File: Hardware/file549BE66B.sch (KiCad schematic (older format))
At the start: 26 parts, among them P21 CONN_01X01, P22 CONN_01X03, P23 CONN_01X01, P24 CONN_01X01, P28 CONN_01X05, U6 CONN_15, U7 LCD-jhd12864e-xl

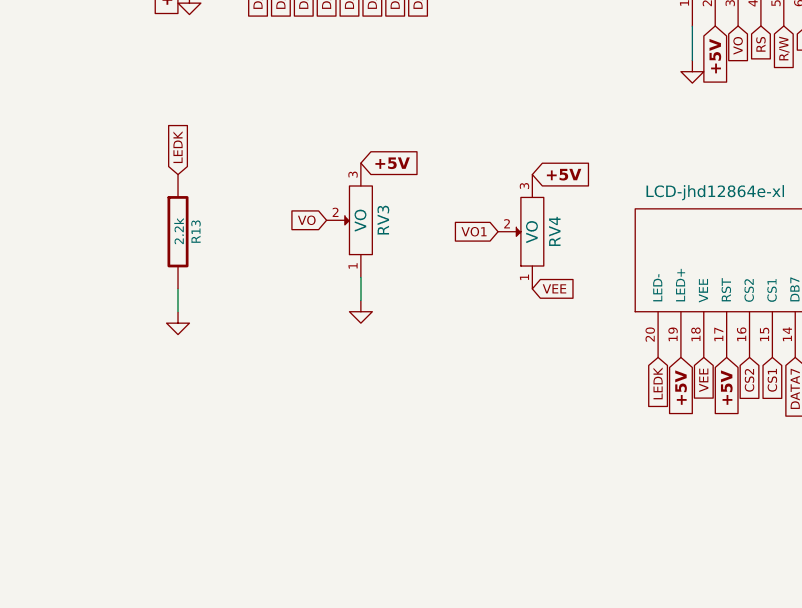
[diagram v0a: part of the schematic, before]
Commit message: verified schematic and component placement
corrections written on schematic and layout
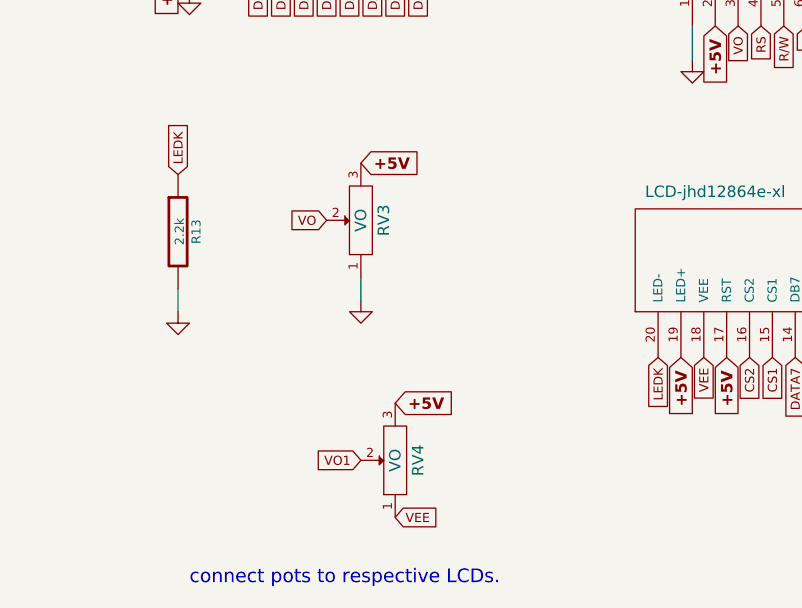
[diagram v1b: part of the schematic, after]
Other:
- note added: "connect pots to respective LCDs."
- moved on the sheet: RV4

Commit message: added new files
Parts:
- removed P21, P23, P24: CONN_01X01, symbol CONN_01X01
- removed U6: CONN_15, symbol CONN_15
- added P31: CONN_01X08, symbol CONN_01X08
- added P32: CONN_01X05, symbol CONN_01X05
- added P?: CONN_01X03, symbol CONN_01X03
- added P?: CONN_01X06, symbol CONN_01X06
- added P?: CONN_01X04, symbol CONN_01X04
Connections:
- net 3.3V: now also P?.1 (P1)
- net CS1: now also P32.2 (P2)
- net CS2: now also P32.1 (P1)
- net DATA0: now also P31.8 (P8)
- net DATA1: now also P31.7 (P7)
- net DATA2: now also P31.6 (P6)
- net DATA3: now also P31.5 (P5)
- net DATA4: now also P31.4 (P4)
- net DATA5: now also P31.3 (P3)
- net DATA6: now also P31.2 (P2)
- net DATA7: now also P31.1 (P1)
- net E: now also P32.3 (P3)
- net GND: now also P?.2 (P2)
- net IN2: now also P?.1 (P1)
- net R/W: now also P32.4 (P4)
- net RS: now also P32.5 (P5)
- net TS: now reaches RV1.2
- net TS: now also P?.3 (P3)
- net POT: now reaches RV2.2
- net POT: now also P?.2 (P2)
- new net: P?.1 (P1), P?.3 (P3)
- new net: P?.2 (P2), P?.4 (P4)
- new net: P?.3 (P3), P?.5 (P5)
- new net: P?.4 (P4), P?.6 (P6)
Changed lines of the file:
@@
 LIBS:contrib
 LIBS:valves
+LIBS:Ultra_DB_X51_v1-cache
+LIBS:16X2-cache
+LIBS:blutooth-cache
 LIBS:MCU_BaseBoard-cache
 EELAYER 25 0
@@
 Text Label 3750 2450 0    50   ~ 0
 IN2
-$Comp
-L CONN_01X01 P21
-U 1 1 555B4642
-P 1400 2400
-F 0 "P21" H 1400 2500 50  0000 C CNN
-F 1 "CONN_01X01" V 1500 2400 50  0000 C CNN
-F 2 "" H 1400 2400 60  0000 C CNN
-F 3 "" H 1400 2400 60  0000 C CNN
-	1    1400 2400
-	1    0    0    -1
-$EndComp
-$Comp
-L CONN_01X01 P23
-U 1 1 555B46A3
-P 2900 2400
-F 0 "P23" H 2900 2500 50  0000 C CNN
-F 1 "CONN_01X01" V 3000 2400 50  0000 C CNN
-F 2 "" H 2900 2400 60  0000 C CNN
-F 3 "" H 2900 2400 60  0000 C CNN
-	1    2900 2400
-	1    0    0    -1
-$EndComp
-$Comp
-L CONN_01X01 P24
-U 1 1 555B4763
-P 4300 2450
-F 0 "P24" H 4300 2550 50  0000 C CNN
-F 1 "CONN_01X01" V 4400 2450 50  0000 C CNN
-F 2 "" H 4300 2450 60  0000 C CNN
-F 3 "" H 4300 2450 60  0000 C CNN
-	1    4300 2450
-	1    0    0    -1
-$EndComp
 Wire Wire Line
 	1050 2400 1200 2400
@@
 	1    0    0    -1
 $EndComp
-$Comp
-L CONN_15 U6
-U 1 1 555B086A
-P 1800 4400
-F 0 "U6" H 1950 4900 60  0000 C CNN
-F 1 "CONN_15" V 2000 4300 60  0000 C CNN
-F 2 "" H 1800 4400 60  0000 C CNN
-F 3 "" H 1800 4400 60  0000 C CNN
-	1    1800 4400
-	0    -1   -1   0
-$EndComp
-$Comp
-L GND #PWR022
-U 1 1 555B0871
-P 1350 4850
-F 0 "#PWR022" H 1350 4850 30  0001 C CNN
-F 1 "GND" H 1350 4780 30  0001 C CNN
-F 2 "" H 1350 4850 60  0001 C CNN
-F 3 "" H 1350 4850 60  0001 C CNN
-	1    1350 4850
-	1    0    0    -1
-$EndComp
-Wire Wire Line
-	1350 4700 1350 4850
-Text GLabel 2350 4700 3    40   Input ~ 0
+Text GLabel 2000 3850 3    40   Input ~ 0
 DATA0
-Text GLabel 2250 4700 3    40   Input ~ 0
+Text GLabel 1900 3850 3    40   Input ~ 0
 DATA1
-Text GLabel 2150 4700 3    40   Input ~ 0
+Text GLabel 1800 3850 3    40   Input ~ 0
 DATA2
-Text GLabel 2050 4700 3    40   Input ~ 0
+Text GLabel 1700 3850 3    40   Input ~ 0
 DATA3
-Text GLabel 1950 4700 3    40   Input ~ 0
+Text GLabel 1600 3850 3    40   Input ~ 0
 DATA4
-Text GLabel 1850 4700 3    40   Input ~ 0
+Text GLabel 1500 3850 3    40   Input ~ 0
 DATA5
-Text GLabel 1750 4700 3    40   Input ~ 0
+Text GLabel 1400 3850 3    40   Input ~ 0
 DATA6
-Text GLabel 1650 4700 3    40   Input ~ 0
+Text GLabel 1300 3850 3    40   Input ~ 0
 DATA7
-Text GLabel 2450 4700 3    40   Input ~ 0
+Text GLabel 2400 3850 3    40   Input ~ 0
 E
-Text GLabel 2550 4700 3    40   Input ~ 0
+Text GLabel 2500 3850 3    40   Input ~ 0
 R/W
-Text GLabel 2650 4700 3    40   Input ~ 0
+Text GLabel 2600 3850 3    40   Input ~ 0
 RS
-Text GLabel 1550 4700 3    40   Input ~ 0
+Text GLabel 2300 3850 3    40   Input ~ 0
 CS1
-Text GLabel 1450 4700 3    40   Input ~ 0
+Text GLabel 2200 3850 3    40   Input ~ 0
 CS2
 $Comp
@@
 $EndComp
 $Comp
-L GND #PWR023
+L GND #PWR022
 U 1 1 555B088B
 P 1300 6250
-F 0 "#PWR023" H 1300 6250 30  0001 C CNN
+F 0 "#PWR022" H 1300 6250 30  0001 C CNN
 F 1 "GND" H 1300 6180 30  0001 C CNN
 F 2 "" H 1300 6250 60  0001 C CNN
@@
 $EndComp
 $Comp
-L GND #PWR024
+L GND #PWR023
 U 1 1 555B0898
 P 2100 6200
-F 0 "#PWR024" H 2100 6200 30  0001 C CNN
+F 0 "#PWR023" H 2100 6200 30  0001 C CNN
 F 1 "GND" H 2100 6130 30  0001 C CNN
 F 2 "" H 2100 6200 60  0001 C CNN
@@
 $EndComp
 $Comp
-L GND #PWR025
+L GND #PWR024
 U 1 1 555B08A8
 P 3550 5150
-F 0 "#PWR025" H 3550 5150 30  0001 C CNN
+F 0 "#PWR024" H 3550 5150 30  0001 C CNN
 F 1 "GND" H 3550 5080 30  0001 C CNN
 F 2 "" H 3550 5150 60  0001 C CNN
@@
 RS
 $Comp
-L GND #PWR026
+L GND #PWR025
 U 1 1 555B08CF
 P 5300 6550
-F 0 "#PWR026" H 5300 6550 30  0001 C CNN
+F 0 "#PWR025" H 5300 6550 30  0001 C CNN
 F 1 "GND" H 5300 6480 30  0001 C CNN
 F 2 "" H 5300 6550 60  0001 C CNN
@@
 Text GLabel 5100 6450 3    40   Input ~ 0
 VO1
-Text GLabel 1250 4700 3    50   Input ~ 10
-+5V
 Text GLabel 3650 5000 3    50   Input ~ 10
 +5V
@@
 Connection ~ 6550 1200
 $Comp
-L GND #PWR027
+L GND #PWR026
 U 1 1 555B17F7
 P 6550 2050
-F 0 "#PWR027" H 6550 2050 30  0001 C CNN
+F 0 "#PWR026" H 6550 2050 30  0001 C CNN
 F 1 "GND" H 6550 1980 30  0001 C CNN
 F 2 "" H 6550 2050 60  0000 C CNN
@@
 Connection ~ 8150 4200
 $Comp
-L GND #PWR028
+L GND #PWR027
 U 1 1 555B1831
 P 8350 4340
-F 0 "#PWR028" H 8350 4340 30  0001 C CNN
+F 0 "#PWR027" H 8350 4340 30  0001 C CNN
 F 1 "GND" H 8350 4270 30  0001 C CNN
 F 2 "" H 8350 4340 60  0000 C CNN
@@
 Connection ~ 6150 3400
 $Comp
-L GND #PWR029
+L GND #PWR028
 U 1 1 555B79B0
 P 6150 3550
-F 0 "#PWR029" H 6150 3550 30  0001 C CNN
+F 0 "#PWR028" H 6150 3550 30  0001 C CNN
 F 1 "GND" H 6150 3480 30  0001 C CNN
 F 2 "" H 6150 3550 60  0000 C CNN
@@
 Text Notes 1350 7450 0    60   ~ 0
 connect pots to respective LCDs.
+$Comp
+L CONN_01X05 P32
+U 1 1 55636DEC
+P 2400 3650
+F 0 "P32" H 2400 3950 50  0000 C CNN
+F 1 "CONN_01X05" V 2500 3650 50  0000 C CNN
+F 2 "" H 2400 3650 60  0000 C CNN
+F 3 "" H 2400 3650 60  0000 C CNN
+	1    2400 3650
+	0    -1   -1   0
+$EndComp
+$Comp
+L CONN_01X08 P31
+U 1 1 55636E71
+P 1650 3650
+F 0 "P31" H 1650 4100 50  0000 C CNN
+F 1 "CONN_01X08" V 1750 3650 50  0000 C CNN
+F 2 "" H 1650 3650 60  0000 C CNN
+F 3 "" H 1650 3650 60  0000 C CNN
+	1    1650 3650
+	0    -1   -1   0
+$EndComp
+$Comp
+L CONN_01X03 P?
+U 1 1 5567F620
+P 3650 1400
+F 0 "P?" H 3650 1600 50  0000 C CNN
+F 1 "CONN_01X03" V 3750 1400 50  0000 C CNN
+F 2 "" H 3650 1400 60  0000 C CNN
+F 3 "" H 3650 1400 60  0000 C CNN
+	1    3650 1400
+	0    1    1    0
+$EndComp
+Text Label 3550 1200 1    40   ~ 0
+TS
+Text Label 3650 1200 1    40   ~ 0
+POT
+Text Label 3750 1200 1    40   ~ 0
+LDR
+Text Label 1200 2400 0    40   ~ 0
+TS
+Text Label 2700 2400 0    40   ~ 0
+POT
+Text Label 4100 2450 0    40   ~ 0
+LDR
+$Comp
+L CONN_01X06 P?
+U 1 1 5569BDE8
+P 6650 4650
+F 0 "P?" H 6650 5000 50  0000 C CNN
+F 1 "CONN_01X06" V 6750 4650 50  0000 C CNN
+F 2 "" H 6650 4650 60  0000 C CNN
+F 3 "" H 6650 4650 60  0000 C CNN
+	1    6650 4650
+	0    -1   -1   0
+$EndComp
+$Comp
+L CONN_01X04 P?
+U 1 1 5569BF4F
+P 6750 5550
+F 0 "P?" H 6750 5800 50  0000 C CNN
+F 1 "CONN_01X04" V 6850 5550 50  0000 C CNN
+F 2 "" H 6750 5550 60  0000 C CNN
+F 3 "" H 6750 5550 60  0000 C CNN
+	1    6750 5550
+	0    -1   -1   0
+$EndComp
+Text GLabel 6400 4900 3    40   Input ~ 8
+3.3V
+Wire Wire Line
+	6400 4850 6400 4900
+$Comp
+L GND #PWR?
+U 1 1 5569C822
+P 6500 5000
+F 0 "#PWR?" H 6500 5000 30  0001 C CNN
+F 1 "GND" H 6500 4930 30  0001 C CNN
+F 2 "" H 6500 5000 60  0000 C CNN
+F 3 "" H 6500 5000 60  0000 C CNN
+	1    6500 5000
+	1    0    0    -1
+$EndComp
+Wire Wire Line
+	6500 4850 6500 5000
+Wire Wire Line
+	6600 4850 6600 5750
+Wire Wire Line
+	6700 4850 6700 5750
+Wire Wire Line
+	6800 4850 6800 5750
+Wire Wire Line
+	6900 4850 6900 5750
 $EndSCHEMATC

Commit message: Added final Files
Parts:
- gave numbers to parts that had none: 3
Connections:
- net 3.3V: now also P18.2 (P2); no longer P18.1 (P1)
- net GND: now also P18.1 (P1); no longer P18.2 (P2)
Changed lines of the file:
@@
 $EndComp
 $Comp
-L CONN_01X03 P?
+L CONN_01X03 P17
 U 1 1 5567F620
 P 3650 1400
-F 0 "P?" H 3650 1600 50  0000 C CNN
+F 0 "P17" H 3650 1600 50  0000 C CNN
 F 1 "CONN_01X03" V 3750 1400 50  0000 C CNN
 F 2 "" H 3650 1400 60  0000 C CNN
@@
 LDR
 $Comp
-L CONN_01X06 P?
+L CONN_01X06 P18
 U 1 1 5569BDE8
 P 6650 4650
-F 0 "P?" H 6650 5000 50  0000 C CNN
+F 0 "P18" H 6650 5000 50  0000 C CNN
 F 1 "CONN_01X06" V 6750 4650 50  0000 C CNN
 F 2 "" H 6650 4650 60  0000 C CNN
@@
 $EndComp
 $Comp
-L CONN_01X04 P?
+L CONN_01X04 P19
 U 1 1 5569BF4F
 P 6750 5550
-F 0 "P?" H 6750 5800 50  0000 C CNN
+F 0 "P19" H 6750 5800 50  0000 C CNN
 F 1 "CONN_01X04" V 6850 5550 50  0000 C CNN
 F 2 "" H 6750 5550 60  0000 C CNN
@@
 	0    -1   -1   0
 $EndComp
-Text GLabel 6400 4900 3    40   Input ~ 8
+Text GLabel 6500 5000 3    40   Input ~ 8
 3.3V
 Wire Wire Line
-	6400 4850 6400 4900
+	6400 4850 6400 5000
 $Comp
-L GND #PWR?
+L GND #PWR029
 U 1 1 5569C822
-P 6500 5000
-F 0 "#PWR?" H 6500 5000 30  0001 C CNN
-F 1 "GND" H 6500 4930 30  0001 C CNN
-F 2 "" H 6500 5000 60  0000 C CNN
-F 3 "" H 6500 5000 60  0000 C CNN
-	1    6500 5000
+P 6400 5000
+F 0 "#PWR029" H 6400 5000 30  0001 C CNN
+F 1 "GND" H 6400 4930 30  0001 C CNN
+F 2 "" H 6400 5000 60  0000 C CNN
+F 3 "" H 6400 5000 60  0000 C CNN
+	1    6400 5000
 	1    0    0    -1
 $EndComp
